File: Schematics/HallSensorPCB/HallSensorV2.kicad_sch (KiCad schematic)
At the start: 3 parts, among them J1 Conn_02x03_Counter_Clockwise, J2 Conn_01x04_Pin

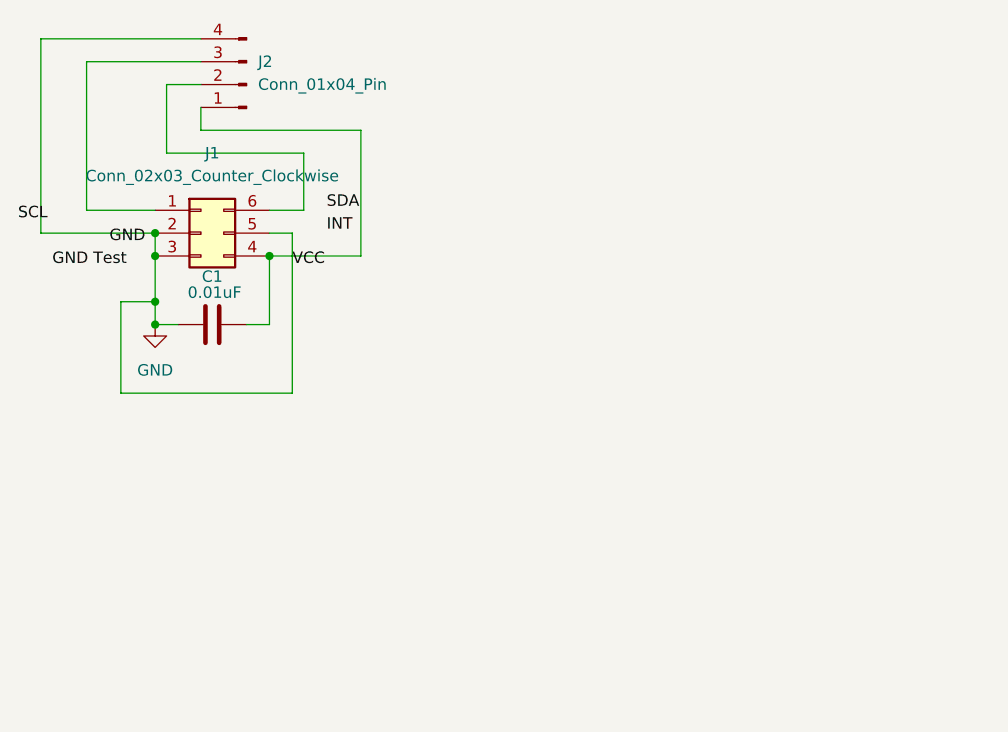
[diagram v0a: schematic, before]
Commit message: Update hall schematic and pcb  - add exact sensor schematic, models, etc  - rerouted traces
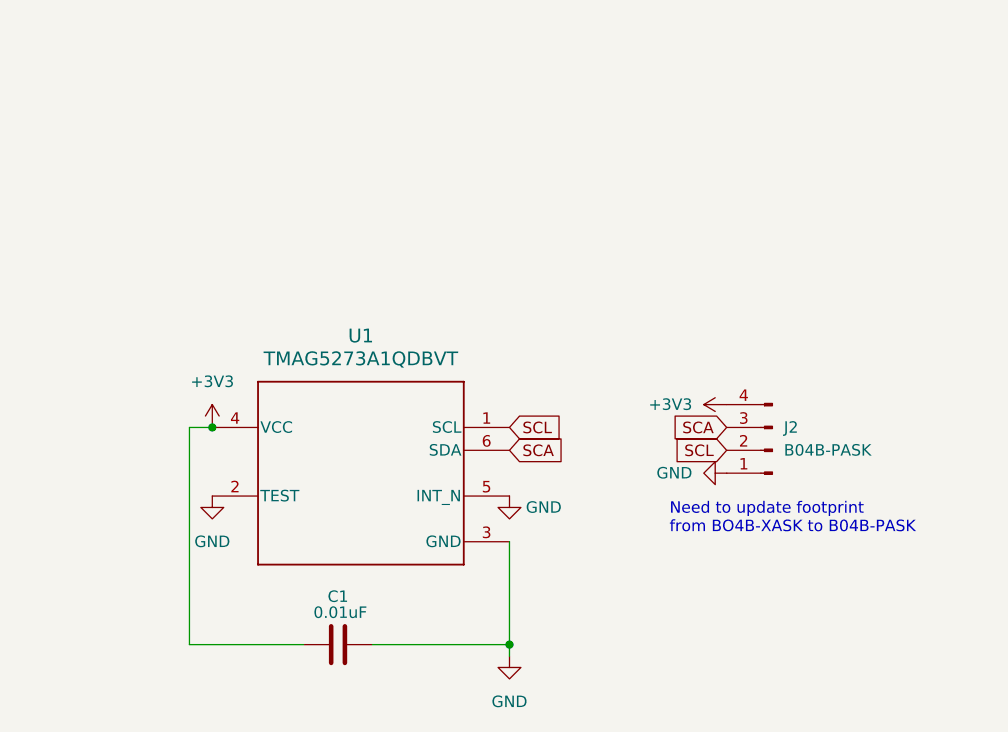
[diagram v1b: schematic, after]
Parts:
- removed J1: Conn_02x03_Counter_Clockwise, footprints:DBV0006A-MFG, symbol Connector_Generic:Conn_02x03_Counter_Clockwise
- added U1: TMAG5273A1QDBVT, DBV0006A-IPC_A, symbol TMAG5273A1QDBVT:TMAG5273A1QDBVT
- C1: footprint (none) -> Capacitor_SMD:C_0805_2012Metric_Pad1.18x1.45mm_HandSolder
- J2: value Conn_01x04_Pin -> B04B-PASK; footprint (none) -> B04B_XASK_1:CONN_B04B-XASK-1_JST
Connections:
- net GND: now also C1.2, J2.1 (Pin_1), U1.2 (TEST), U1.3 (GND), U1.5 (INT_N); no longer C1.1, J2.4 (Pin_4)
- net SCL: now also J2.2 (Pin_2), U1.1 (SCL)
- net SCA: now reaches J2.3 (Pin_3)
- net SCA: now also U1.6 (SDA)
- new net +3V3: C1.1, J2.4 (Pin_4), U1.4 (VCC)
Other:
- note added: "Need to update footprint from BO4B-XASK to B04B-PASK"
